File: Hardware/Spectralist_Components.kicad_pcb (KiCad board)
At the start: 4 copper layers, 60 x 100 mm, 103 parts, among them J1 Conn_01x08_Pin, J2 Conn_01x08_Pin, J3 Conn_01x10_Pin, J4 Conn_01x10_Pin, J5 Eurorack_10_pin_power, J6 SWD_Header, J7 Conn_01x02_Pin, J8 USB_B_Micro, U1 STM32H723VGTx, U2 PCM5100APW, U3 TPS561201, U4 LT1117-3.3, U5 MCP6004, U6 STF202-22T1G, U7 MCP6004, U8 TL072, Y1 8MHz 20pF

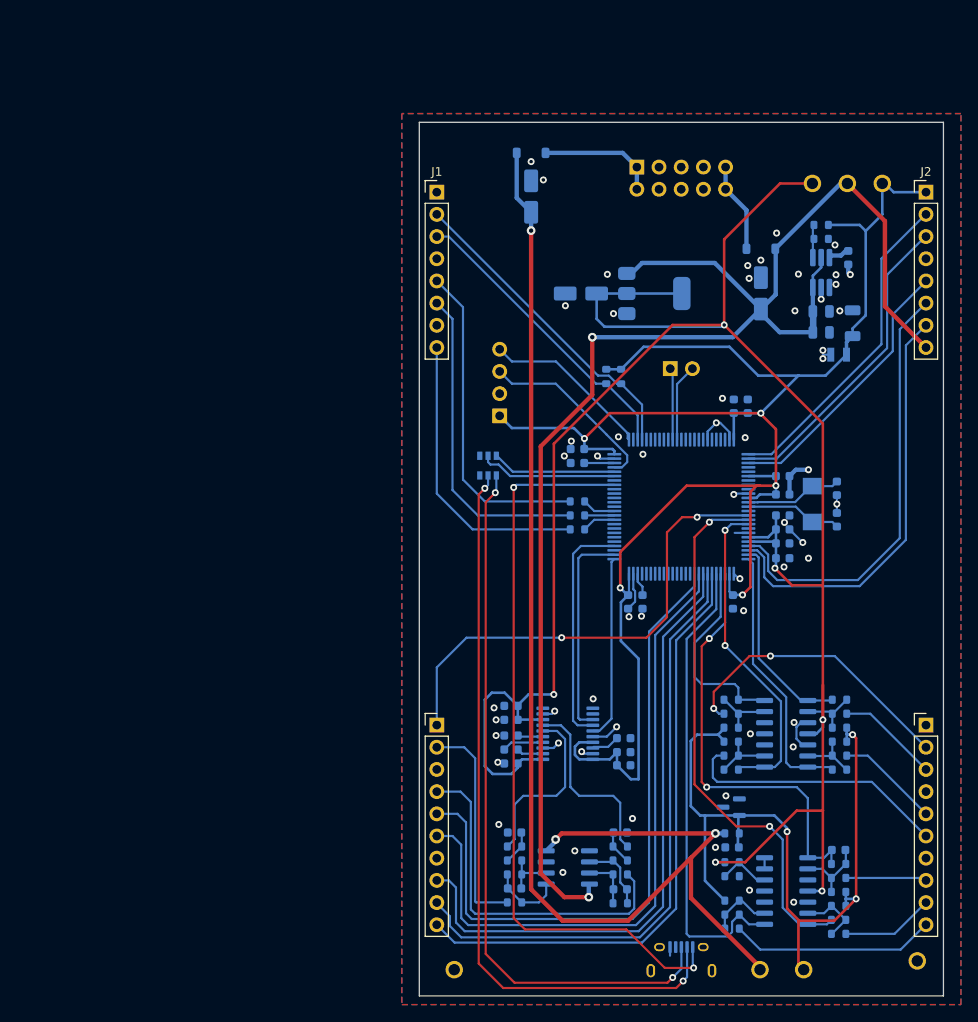
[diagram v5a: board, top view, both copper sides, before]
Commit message: Started adding JLC part numbers
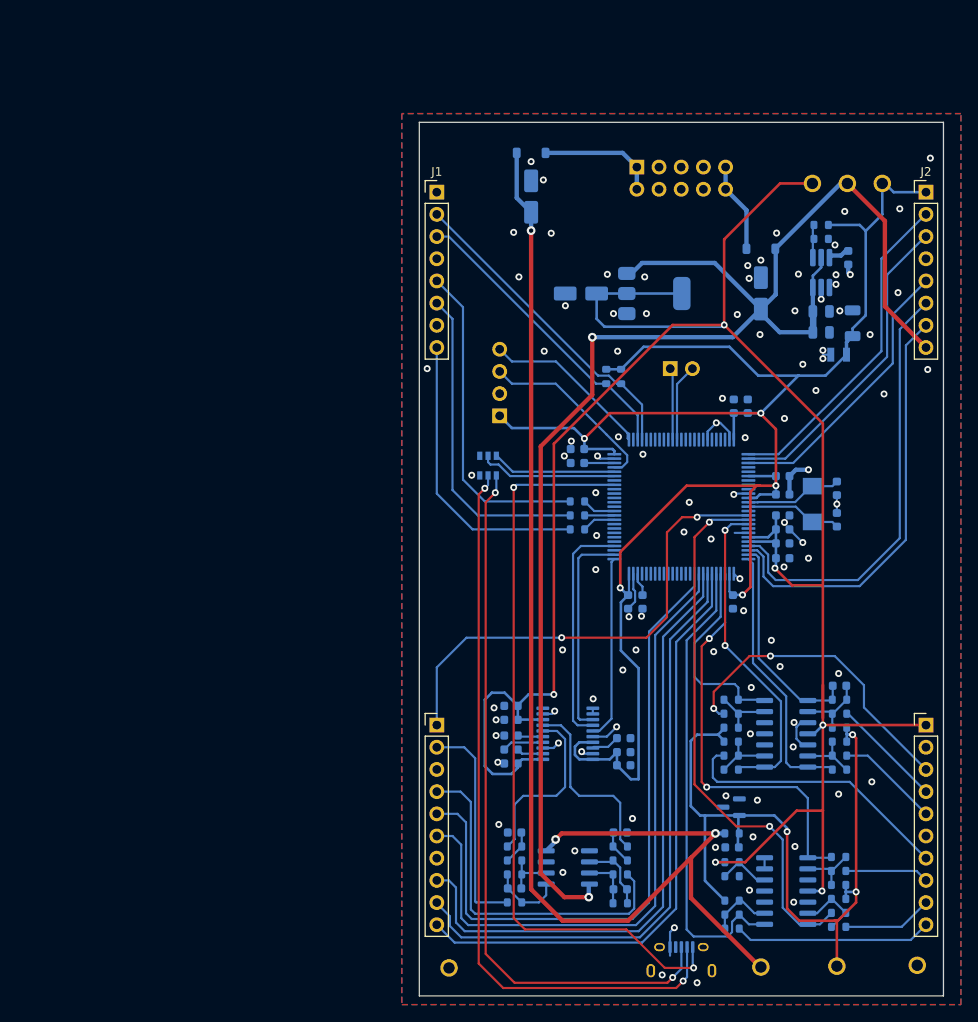
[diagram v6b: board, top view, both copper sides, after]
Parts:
- J7: value Conn_01x02_Pin -> UART_Test_Pins
- R10, R9: value 1k -> 100
- moved C35 18.8 mm to (148.1, 114.5)
- moved TP7 3.82 mm to (147.8, 146.6)
- moved R17 0.80 mm to (148.0, 142.1)
- moved R19 0.80 mm to (148.0, 140.5)
- moved R23 0.80 mm to (148.0, 135.7)
- moved R24 0.80 mm to (148.0, 134.1)
- moved R16 0.80 mm to (148.0, 138.9)
- moved R22 0.80 mm to (148.0, 137.3)
- moved TP4 0.63 mm to (103.4, 146.8)
- moved TP8 0.50 mm to (157.0, 146.5)
- moved TP3 0.32 mm to (139.1, 146.7)
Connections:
- C35 pad 2: Net-(U5A--) -> Net-(U7A--)
- J3 pad 1: /Filter_B_Pot -> /Filter_B_Trm
- J3 pad 10: /Harm_Warp_Pot -> /Harm_Stretch_Pot
- J3 pad 5: /Filter_Slope_Pot -> /Filter_B_Pot
- J3 pad 6: /Filter_B_Trm -> /Filter_Slope_Pot
- J3 pad 8: /Harm_Stretch_Trm -> /Harm_Warp_Pot
- J3 pad 9: /Harm_Stretch_Pot -> /Harm_Stretch_Trm
- J4 pad 1: GND -> +3.3VA
- J4 pad 10: /Filter_A_CV_In -> /Filter_B_CV_In
- J4 pad 2: /Harm_Warp_CV_In -> GND
- J4 pad 3: /Filter_B_CV_In -> /Harm_Stretch_CV_In
- J4 pad 4: GND -> /Pitch_CV_In
- J4 pad 6: /Pan_CV_In -> GND
- J4 pad 7: GND -> /Filter_A_CV_In
- J4 pad 8: /Pitch_CV_In -> /Harm_Warp_CV_In
- J4 pad 9: /Harm_Stretch_CV_In -> /Pan_CV_In
- R12 pad 2: /Pan_CV_In -> /Filter_A_CV_In
- R17 pad 2: /Harm_Stretch_CV_In -> /Pan_CV_In
- R19 pad 1: /Harm_Stretch_CV -> /Pan_CV
- R21 pad 1: /Pan_CV -> /Filter_A_CV
- R23 pad 2: /Pitch_CV_In -> /Harm_Warp_CV_In
- R24 pad 1: /Pitch_CV_Scaled -> /Harm_Warp_CV
- R26 pad 2: /Harm_Warp_CV_In -> /Harm_Stretch_CV_In
- R27 pad 1: /Harm_Warp_CV -> /Harm_Stretch_CV
- R32 pad 2: /Filter_A_CV_In -> /Filter_B_CV_In
- R33 pad 1: /Filter_A_CV -> /Filter_B_CV
- R35 pad 2: /Filter_B_CV_In -> /Pitch_CV_In
- R36 pad 1: /Filter_B_CV -> /Pitch_CV_Scaled
- U1 pad 15: /Filter_B_Pot -> /Filter_B_Trm
- U1 pad 16: /Harm_Stretch_CV -> /Pan_CV
- U1 pad 17: /Pan_CV -> /Filter_A_CV
- U1 pad 24: /Filter_B_CV -> /Pitch_CV_Scaled
- U1 pad 28: /Pitch_CV_Scaled -> /Harm_Warp_CV
- U1 pad 29: /Harm_Warp_CV -> /Harm_Stretch_CV
- U1 pad 30: /Filter_A_CV -> /Filter_B_CV
- U1 pad 31: /Harm_Warp_Pot -> /Harm_Stretch_Pot
- U1 pad 32: /Harm_Stretch_Pot -> /Harm_Stretch_Trm
- U1 pad 33: /Harm_Stretch_Trm -> /Harm_Warp_Pot
- U1 pad 34: /Filter_B_Trm -> /Filter_Slope_Pot
- U1 pad 35: /Filter_Slope_Pot -> /Filter_B_Pot
- U5 pad 1: /Pitch_CV_Scaled -> /Harm_Warp_CV
- U5 pad 7: /Harm_Stretch_CV -> /Pan_CV
- U5 pad 8: /Filter_A_CV -> /Filter_B_CV
- U7 pad 1: /Filter_B_CV -> /Pitch_CV_Scaled
- U7 pad 14: /Harm_Warp_CV -> /Harm_Stretch_CV
- U7 pad 8: /Pan_CV -> /Filter_A_CV
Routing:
- net /Harm_Stretch_CV: track 62.4 -> 23.1 mm, vias 2 -> 0
- net /Filter_B_CV: track 23.3 -> 53.6 mm
- net /Harm_Stretch_CV_In: track 10.7 -> 36.2 mm, vias 0 -> 2
- net /Pan_CV: track 37.3 -> 62.7 mm
- net /Pitch_CV_Scaled: track 49.4 -> 24.9 mm, vias 2 -> 0
- net /Harm_Warp_CV: track 23.1 -> 47.4 mm, vias 0 -> 2
- net /Harm_Warp_CV_In: track 33.6 -> 9.62 mm, vias 2 -> 0
- net /Filter_B_Pot: track 55.2 -> 75.9 mm, vias 2 -> 0
- net /Pan_CV_In: track 30.7 -> 10.3 mm
- net /Filter_B_Trm: track 75.2 -> 55.2 mm, vias 0 -> 2
- net /Filter_A_CV: track 53.9 -> 37.3 mm, vias 0 -> 2
- net +3.3VA: track 246.9 -> 258.3 mm
- net /Filter_B_CV_In: track 11.7 -> 22.6 mm
- net /Filter_A_CV_In: track 23.5 -> 31.8 mm
- net /Pitch_CV_In: track 9.29 -> 12.8 mm
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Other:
- board text added: "J1"
- board text added: "J2"

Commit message: v1.0 PCBs sent to production
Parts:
- J7: footprint Connector_PinHeader_2.54mm:PinHeader_1x02_P2.54mm_Vertical -> Connector_PinHeader_2.54mm:PinHeader_1x03_P2.54mm_Vertical
- R12, R17, R20, R23, R26, R32, R35: value 82k -> 100k
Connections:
- J7 pad 1: /UART_TX -> /SPI3_NSS
- J7 pad 2: /UART_RX -> /UART_TX
- U1 pad 77: unconnected-(U1-PA15(JTDI)-Pad77) -> /SPI3_NSS
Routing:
- net /SPI3_NSS: track 0.00 -> 13.8 mm, vias 0 -> 1
- net GND: track 41.2 -> 48.4 mm, vias 97 -> 115
- net /UART_RX: track 8.86 -> 9.91 mm
- net /UART_TX: track 8.24 -> 9.06 mm
- net /LED_Filter_B_Out: track 33.7 -> 34.5 mm
- net /LED_Oct_Out: track 36.8 -> 37.5 mm
- net /LED_Filter_A_Out: track 37.3 -> 38.0 mm
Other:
- board text added: "CS"

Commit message: Code tidy up; implementing CV , pots and trimmers
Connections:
- J3 pad 10: /Harm_Stretch_Pot -> /Harm_Warp_Pot
- J3 pad 8: /Harm_Warp_Pot -> /Harm_Stretch_Pot
- U1 pad 31: /Harm_Stretch_Pot -> /Harm_Warp_Pot
- U1 pad 33: /Harm_Warp_Pot -> /Harm_Stretch_Pot
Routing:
- net /Harm_Warp_Pot: track 71.8 -> 69.9 mm
- net /Harm_Stretch_Pot: track 69.9 -> 71.8 mm
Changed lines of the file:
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@@
 			(layers "*.Cu" "*.Mask")
 			(remove_unused_layers no)
-			(net 34 "/Harm_Warp_Pot")
+			(net 41 "/Harm_Stretch_Pot")
 			(pinfunction "Pin_8")
 			(pintype "passive")
@@
 			(layers "*.Cu" "*.Mask")
 			(remove_unused_layers no)
-			(net 41 "/Harm_Stretch_Pot")
+			(net 34 "/Harm_Warp_Pot")
 			(pinfunction "Pin_10")
 			(pintype "passive")
@@
 			(layers "B.Cu" "B.Paste" "B.Mask")
 			(roundrect_rratio 0.25)
-			(net 41 "/Harm_Stretch_Pot")
+			(net 34 "/Harm_Warp_Pot")
 			(pinfunction "PA7")
 			(pintype "bidirectional")
@@
 			(layers "B.Cu" "B.Paste" "B.Mask")
 			(roundrect_rratio 0.25)
-			(net 34 "/Harm_Warp_Pot")
+			(net 41 "/Harm_Stretch_Pot")
 			(pinfunction "PC5")
 			(pintype "bidirectional")
@@
 	)
 	(segment
-		(start 104.2 141.6)
-		(end 104.2 137.6)
-		(width 0.25)
-		(layer "B.Cu")
-		(net 34)
-	)
-	(segment
-		(start 127.9 139.8)
-		(end 125.1 142.6)
-		(width 0.25)
-		(layer "B.Cu")
-		(net 34)
-	)
-	(segment
-		(start 132.5 104.3)
-		(end 127.9 108.9)
-		(width 0.25)
-		(layer "B.Cu")
-		(net 34)
-	)
-	(segment
-		(start 103.38 136.78)
-		(end 102 136.78)
+		(start 133.5 105.4)
+		(end 129.4 109.5)
 		(width 0.25)
 		(layer "B.Cu")
@@
 	)
 	(segment
-		(start 104.2 137.6)
-		(end 103.38 136.78)
+		(start 129.4 109.5)
+		(end 129.4 140)
 		(width 0.25)
 		(layer "B.Cu")
@@
 	)
 	(segment
-		(start 127.9 108.9)
-		(end 127.9 139.8)
+		(start 129.4 140)
+		(end 125.5 143.9)
 		(width 0.25)
 		(layer "B.Cu")
@@
 	)
 	(segment
-		(start 132.5 101.675)
-		(end 132.5 104.3)
+		(start 104.04 143.9)
+		(end 102 141.86)
 		(width 0.25)
 		(layer "B.Cu")
@@
 	)
 	(segment
-		(start 125.1 142.6)
-		(end 105.2 142.6)
+		(start 125.5 143.9)
+		(end 104.04 143.9)
 		(width 0.25)
 		(layer "B.Cu")
@@
 	)
 	(segment
-		(start 105.2 142.6)
-		(end 104.2 141.6)
+		(start 133.5 101.675)
+		(end 133.5 105.4)
 		(width 0.25)
 		(layer "B.Cu")
@@
 	)
 	(segment
-		(start 133.5 105.4)
-		(end 129.4 109.5)
+		(start 104.2 141.6)
+		(end 104.2 137.6)
 		(width 0.25)
 		(layer "B.Cu")
@@
 	)
 	(segment
-		(start 129.4 109.5)
-		(end 129.4 140)
+		(start 127.9 139.8)
+		(end 125.1 142.6)
 		(width 0.25)
 		(layer "B.Cu")
@@
 	)
 	(segment
-		(start 129.4 140)
-		(end 125.5 143.9)
+		(start 132.5 104.3)
+		(end 127.9 108.9)
 		(width 0.25)
 		(layer "B.Cu")
@@
 	)
 	(segment
-		(start 104.04 143.9)
-		(end 102 141.86)
+		(start 103.38 136.78)
+		(end 102 136.78)
 		(width 0.25)
 		(layer "B.Cu")
@@
 	)
 	(segment
-		(start 125.5 143.9)
-		(end 104.04 143.9)
+		(start 104.2 137.6)
+		(end 103.38 136.78)
 		(width 0.25)
 		(layer "B.Cu")
@@
 	)
 	(segment
-		(start 133.5 101.675)
-		(end 133.5 105.4)
+		(start 127.9 108.9)
+		(end 127.9 139.8)
+		(width 0.25)
+		(layer "B.Cu")
+		(net 41)
+	)
+	(segment
+		(start 132.5 101.675)
+		(end 132.5 104.3)
+		(width 0.25)
+		(layer "B.Cu")
+		(net 41)
+	)
+	(segment
+		(start 125.1 142.6)
+		(end 105.2 142.6)
+		(width 0.25)
+		(layer "B.Cu")
+		(net 41)
+	)
+	(segment
+		(start 105.2 142.6)
+		(end 104.2 141.6)
 		(width 0.25)
 		(layer "B.Cu")
